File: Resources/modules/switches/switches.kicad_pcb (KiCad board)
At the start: 2 copper layers, 50 x 90 mm, 45 parts, among them J1 switchesOut, J10 Conn_01x01_Female, J11 Conn_01x01_Female, J12 Conn_01x01_Female, J2 Conn_01x01_Female, J3 Conn_01x01_Female, J4 Conn_01x01_Female, J5 Conn_01x01_Female, J6 Conn_01x01_Female, J7 Conn_01x01_Female, J8 Conn_01x01_Female, J9 Conn_01x01_Female, Q1 2N7002, Q2 2N7002, Q3 2N7002, Q4 2N7002, Q5 2N7002, Q6 2N7002

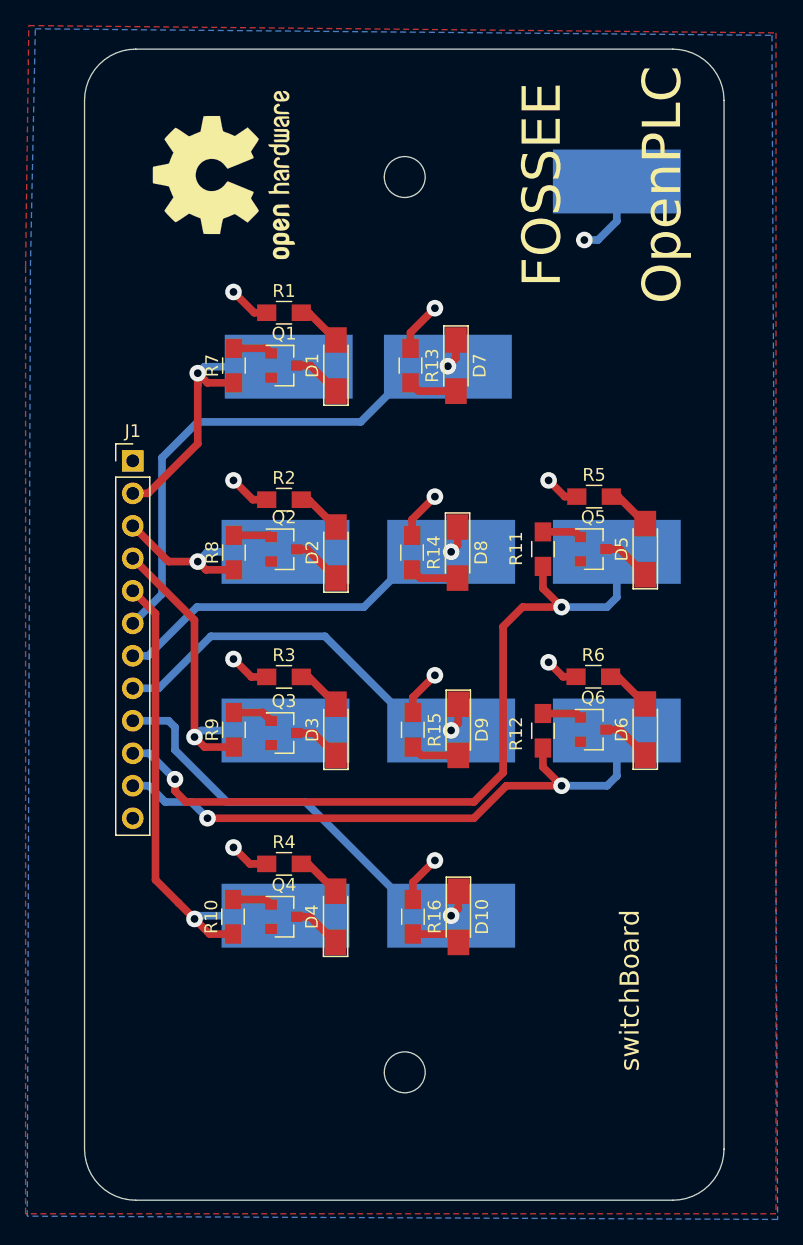
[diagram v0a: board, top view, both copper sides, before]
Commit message: altered switches-board design; shifted resistor
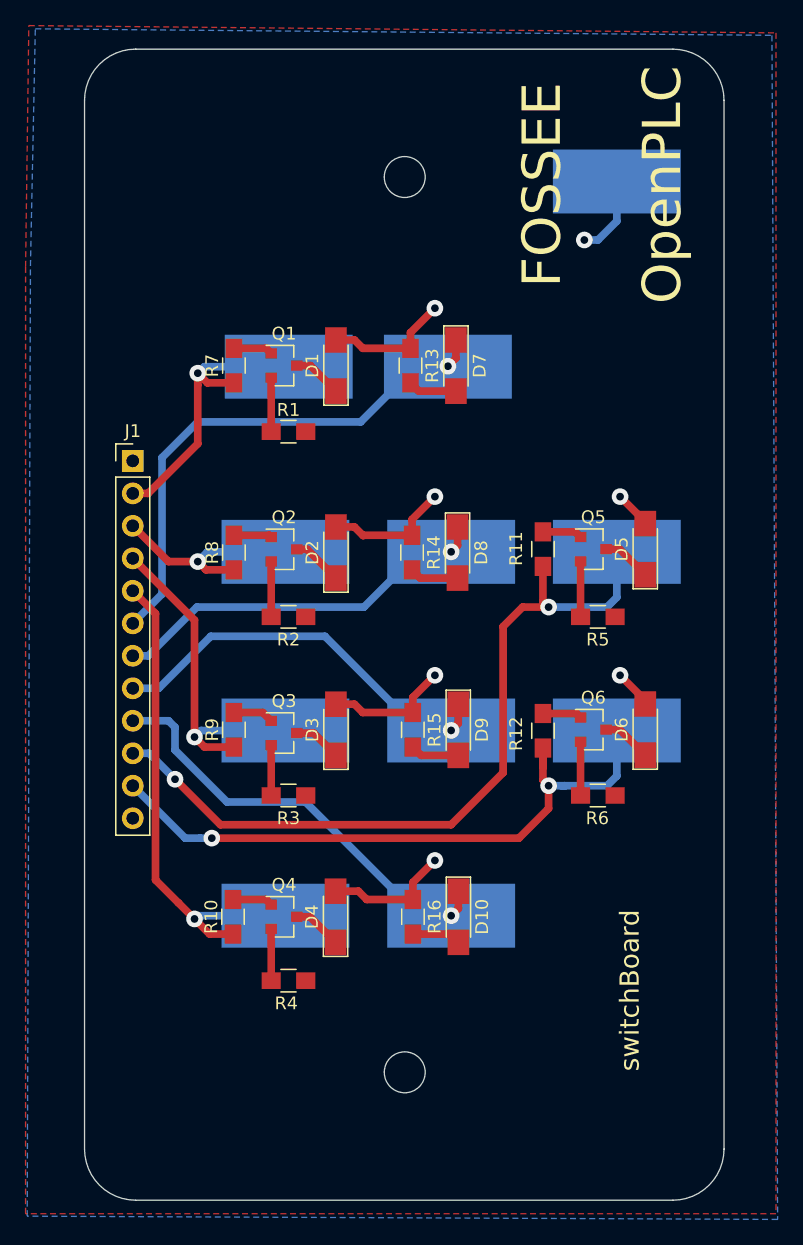
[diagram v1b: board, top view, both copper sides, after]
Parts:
- removed REF***: OSHW-Logo2_14.6x12mm_SilkScreen, Symbols:OSHW-Logo2_14.6x12mm_SilkScreen
- moved R5 9.40 mm to (134.2, 95.8)
- moved R1 9.31 mm to (110.0, 81.3)
- moved R6 9.29 mm to (134.2, 109.7)
- moved R3 9.28 mm to (110.0, 109.7)
- moved R2 9.17 mm to (110.0, 95.8)
- moved R4 9.14 mm to (110.0, 124.2)
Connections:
- D1 pad 2: Net-(D1-Pad2) -> +5V
- D2 pad 2: Net-(D2-Pad2) -> +5V
- D3 pad 2: Net-(D3-Pad2) -> +5V
- D4 pad 2: Net-(D4-Pad2) -> +5V
- D5 pad 2: Net-(D5-Pad2) -> +5V
- D6 pad 2: Net-(D6-Pad2) -> +5V
- Q1 pad 2: GND -> Net-(Q1-Pad2)
- Q2 pad 2: GND -> Net-(Q2-Pad2)
- Q3 pad 2: GND -> Net-(Q3-Pad2)
- Q4 pad 2: GND -> Net-(Q4-Pad2)
- Q5 pad 2: GND -> Net-(Q5-Pad2)
- Q6 pad 2: GND -> Net-(Q6-Pad2)
- R1 pad 1: +5V -> Net-(Q1-Pad2)
- R1 pad 2: Net-(D1-Pad2) -> GND
- R2 pad 1: +5V -> Net-(Q2-Pad2)
- R2 pad 2: Net-(D2-Pad2) -> GND
- R3 pad 1: +5V -> Net-(Q3-Pad2)
- R3 pad 2: Net-(D3-Pad2) -> GND
- R4 pad 1: +5V -> Net-(Q4-Pad2)
- R4 pad 2: Net-(D4-Pad2) -> GND
- R5 pad 1: +5V -> Net-(Q5-Pad2)
- R5 pad 2: Net-(D5-Pad2) -> GND
- R6 pad 1: +5V -> Net-(Q6-Pad2)
- R6 pad 2: Net-(D6-Pad2) -> GND
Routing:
- net +5V: track 33.2 -> 46.0 mm, vias 10 -> 6
- net Net-(Q5-Pad2): track 0.00 -> 4.34 mm
- net Net-(Q2-Pad2): track 0.00 -> 4.33 mm
- net Net-(Q1-Pad2): track 0.00 -> 4.22 mm
- net Net-(Q6-Pad2): track 0.00 -> 4.20 mm
- net Net-(Q4-Pad2): track 0.00 -> 4.05 mm
- net Net-(Q3-Pad2): track 0.00 -> 3.93 mm
- net /s10: track 47.4 -> 51.0 mm
- net Net-(D6-Pad2): track 3.59 -> 0.00 mm
- net Net-(D3-Pad2): track 3.59 -> 0.00 mm
- net Net-(D2-Pad2): track 3.59 -> 0.00 mm
- net Net-(D1-Pad2): track 3.59 -> 0.00 mm
- net Net-(D4-Pad2): track 3.56 -> 0.00 mm
- net Net-(D5-Pad2): track 3.52 -> 0.00 mm
- net /s9: track 60.6 -> 61.1 mm

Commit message: label correction&additions in traffic&switches modules. Updated gerbers - both V1 and modules
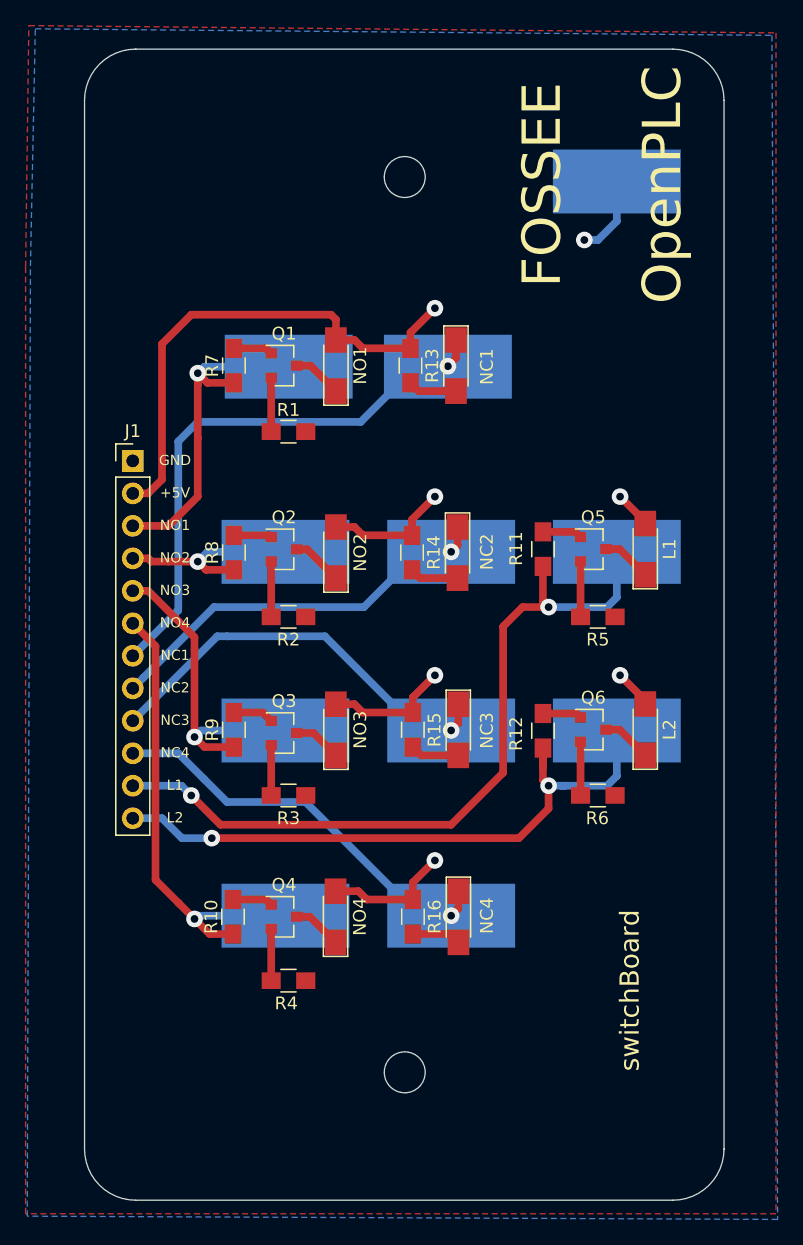
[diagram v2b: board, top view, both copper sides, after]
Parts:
- D1: value LED -> NO1
- D10: value LED -> NC4
- D2: value LED -> NO2
- D3: value LED -> NO3
- D4: value LED -> NO4
- D5: value LED -> L1
- D6: value LED -> L2
- D7: value LED -> NC1
- D8: value LED -> NC2
- D9: value LED -> NC3
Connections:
- J1 pad 10: /s9 -> /s8
- J1 pad 11: /s10 -> /s9
- J1 pad 12: +5V -> /s10
- J1 pad 2: /s1 -> +5V
- J1 pad 3: /s2 -> /s1
- J1 pad 4: /s3 -> /s2
- J1 pad 5: /s4 -> /s3
- J1 pad 6: /s5 -> /s4
- J1 pad 7: /s6 -> /s5
- J1 pad 8: /s7 -> /s6
- J1 pad 9: /s8 -> /s7
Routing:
- net +5V: track 46.0 -> 75.6 mm
- net /s1: track 22.7 -> 26.1 mm
- net /s4: track 38.4 -> 35.8 mm
- net /s5: track 41.5 -> 44.0 mm
- net /s8: track 34.4 -> 32.3 mm
- net /s3: track 26.7 -> 24.9 mm
- net /s9: track 61.1 -> 60.1 mm
- net /s6: track 30.4 -> 31.5 mm
- net /s2: track 16.5 -> 15.5 mm
- net /s10: track 51.0 -> 50.0 mm
- net /s7: track 31.9 -> 33.0 mm
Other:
- board text added: "+5V"
- board text added: "GND"
- board text added: "L1"
- board text added: "L2"
- board text added: "NC1"
- board text added: "NC2"
- board text added: "NC3"
- board text added: "NC4"
- board text added: "NO1"
- board text added: "NO2"
- board text added: "NO3"
- board text added: "NO4"
